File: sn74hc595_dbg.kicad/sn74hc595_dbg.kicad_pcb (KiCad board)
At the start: 2 copper layers, 27.7 x 42.8 mm, 12 parts, among them J1 Conn_01x04, J2 Conn_01x04, U2 74HC595

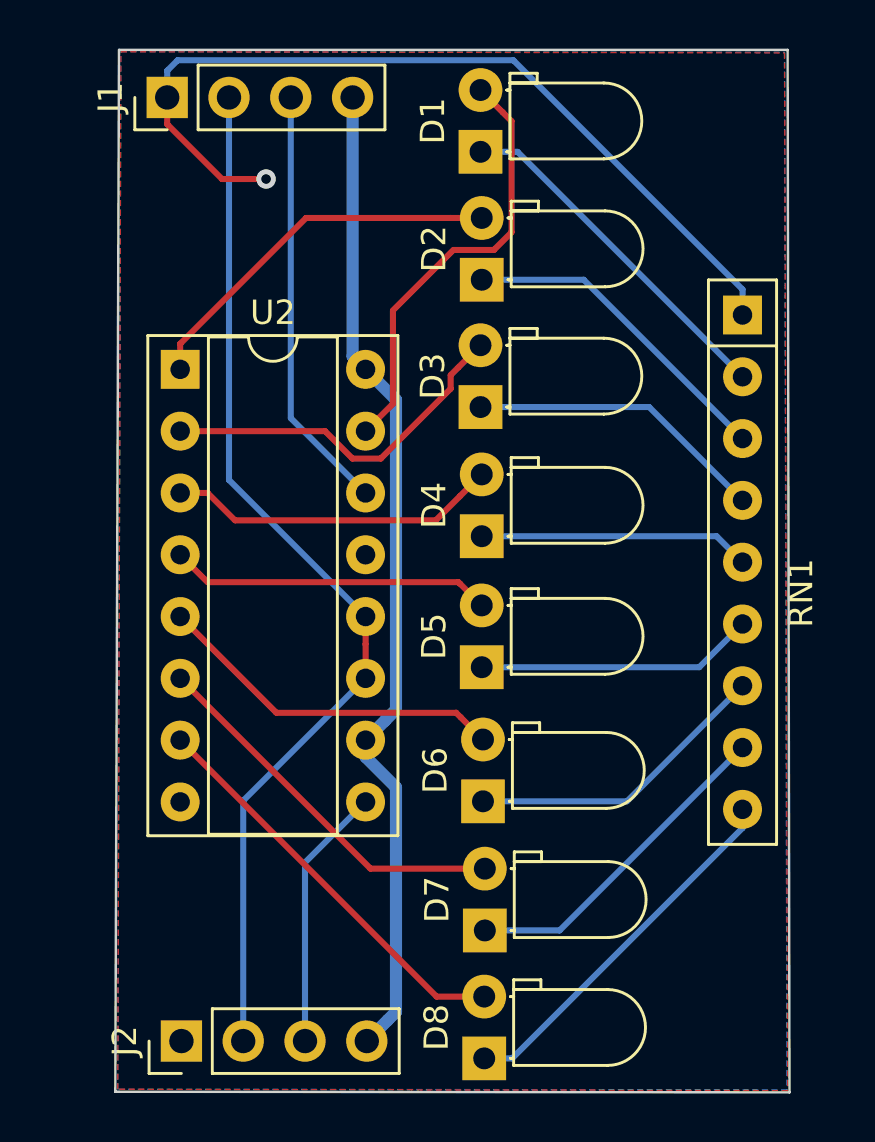
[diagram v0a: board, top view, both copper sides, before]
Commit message: swapped horizontal LEDs with vertical LEDs
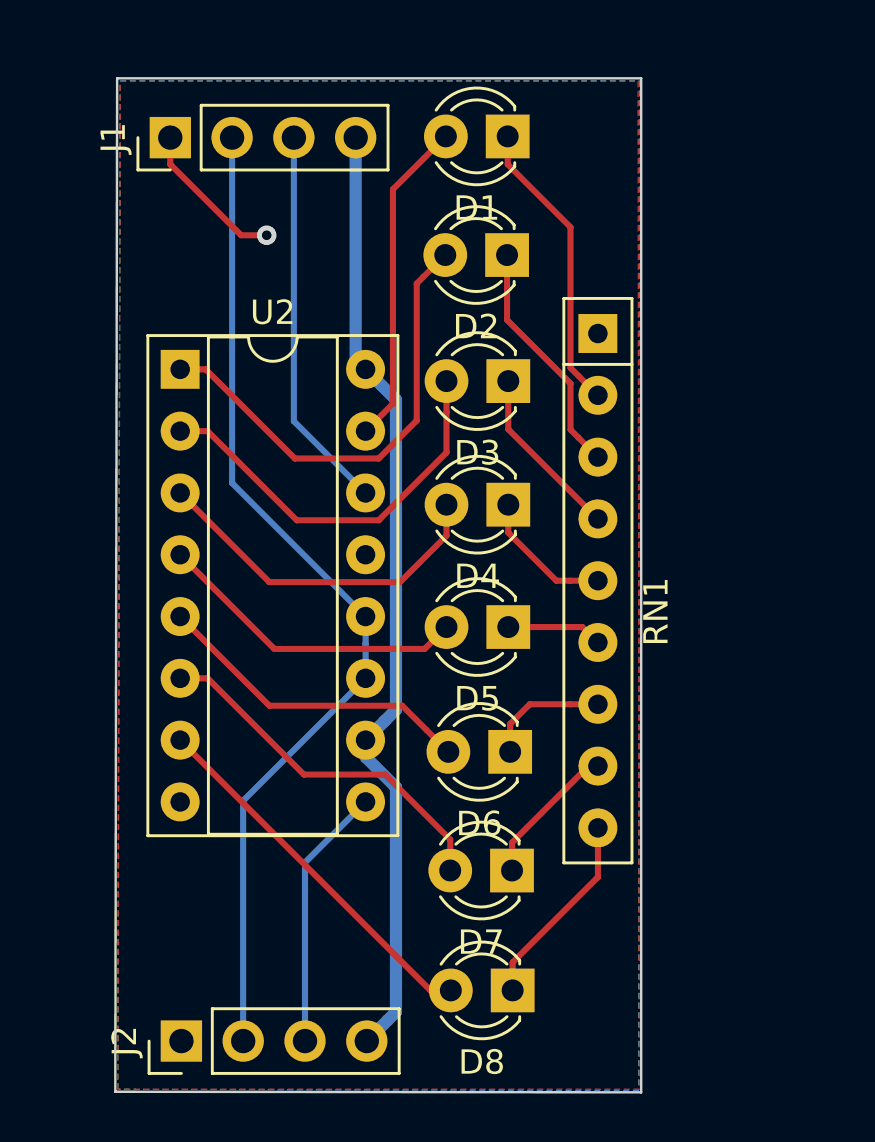
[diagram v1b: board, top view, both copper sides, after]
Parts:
- D1, D2, D3, D4, D5, D6, D7, D8: footprint LED_THT:LED_D3.0mm_Horizontal_O1.27mm_Z2.0mm_Clear -> LED_THT:LED_D3.0mm
- moved RN1 5.99 mm to (103.3, 57.9)
- moved D8 3.03 mm to (99.8, 84.9), turned to 180 degrees
- moved D7 2.71 mm to (99.7, 80.0), turned to 180 degrees
- moved D6 2.32 mm to (99.7, 75.1), turned to 180 degrees
- moved D5 1.98 mm to (99.6, 70.0), turned to 180 degrees
- moved D4 1.69 mm to (99.6, 65.0), turned to 180 degrees
- moved J1 1.66 mm to (85.7, 49.9)
- moved D3 1.56 mm to (99.6, 59.9), turned to 180 degrees
- moved D2 1.45 mm to (99.5, 54.7), turned to 180 degrees
- moved D1 1.29 mm to (99.6, 49.8), turned to 180 degrees
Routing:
- net GND: track 36.0 -> 6.27 mm
- net Net-(D7-Pad1): track 13.7 -> 5.98 mm
- net Net-(D6-Pad1): track 12.6 -> 5.09 mm
- net Net-(D5-Pad1): track 11.5 -> 3.95 mm
- net Net-(D8-Pad1): track 15.3 -> 8.13 mm
- net Net-(D4-Pad1): track 11.2 -> 5.65 mm
- net Net-(D3-Pad1): track 12.4 -> 7.19 mm
- net Net-(D1-Pad2): track 18.0 -> 13.5 mm
- net Net-(D2-Pad2): track 15.6 -> 19.2 mm
- net Net-(D2-Pad1): track 13.4 -> 9.85 mm
- net Net-(D1-Pad1): track 14.6 -> 12.2 mm
- net Net-(J1-Pad3): track 17.5 -> 15.8 mm
- net +5V: track 41.1 -> 39.4 mm
- net Net-(J1-Pad2): track 43.2 -> 41.5 mm
- net Net-(D3-Pad2): track 15.1 -> 16.6 mm
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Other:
- board size 27.7 x 42.8 mm -> 21.6 x 41.7 mm

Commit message: optimized layout, added labels
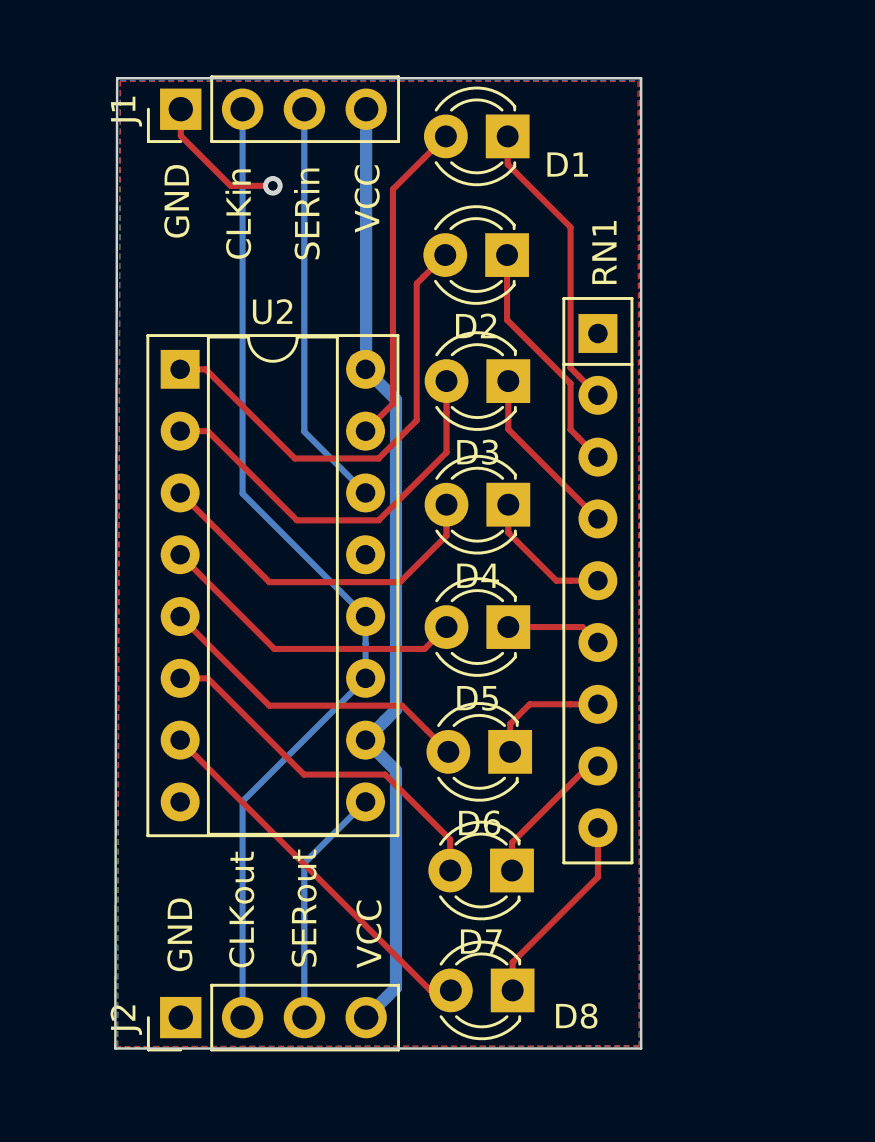
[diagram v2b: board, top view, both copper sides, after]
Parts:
- moved J1 1.25 mm to (86.1, 48.7)
- moved J2 0.97 mm to (86.1, 86.1)
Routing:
- net Net-(J1-Pad3): track 15.8 -> 16.8 mm
- net Net-(J2-Pad3): track 10.9 -> 9.91 mm
- net +5V: track 39.4 -> 40.0 mm
- net GND: track 6.27 -> 5.73 mm
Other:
- board size 21.6 x 41.7 mm -> 21.6 x 39.9 mm
- board text added: "CLKin"
- board text added: "CLKout"
- board text added: "GND"
- board text added: "Rev 1"
- board text added: "SERin"
- board text added: "SERout"
- board text added: "VCC"
- board text added: "https://github.com/ bablokb/pic-toolchain/ src/sn74hc595_dbg"

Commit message: Rev 2: connector for output-pins / jumper for SCLK/RCLK connection
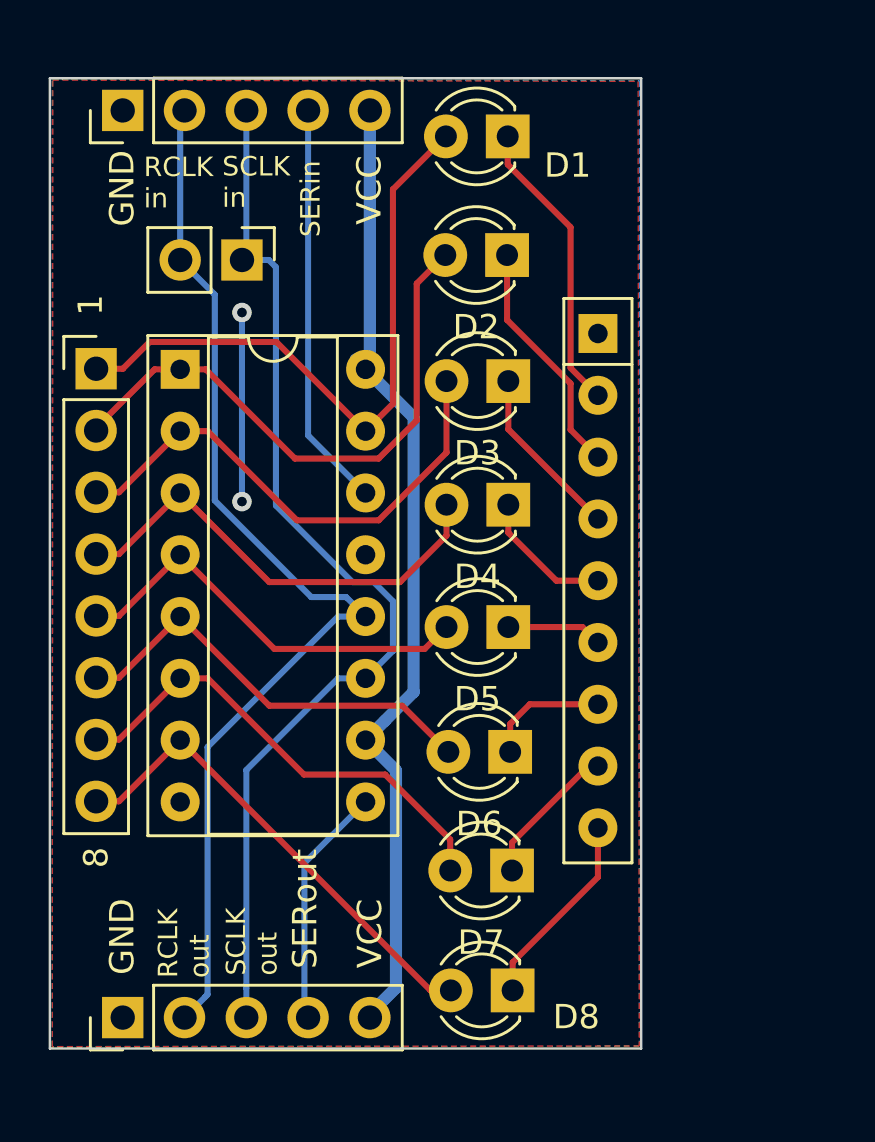
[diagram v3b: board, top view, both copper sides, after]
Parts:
- added J3: Jumper, Connector_PinHeader_2.54mm:PinHeader_1x02_P2.54mm_Vertical, F.Cu at (88.6, 54.9)
- added J4: Conn_01x08_Male, Connector_PinHeader_2.54mm:PinHeader_1x08_P2.54mm_Vertical, F.Cu at (82.7, 59.4)
- J1, J2: value Conn_01x04 -> Conn_01x05; footprint Connector_PinHeader_2.54mm:PinHeader_1x04_P2.54mm_Vertical -> Connector_PinHeader_2.54mm:PinHeader_1x05_P2.54mm_Vertical
- RN1: value R_Network08 -> 680
- moved J1 2.39 mm to (83.7, 48.8)
- moved J2 2.39 mm to (83.7, 86.1)
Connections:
- net Net-(D1-Pad2) renamed /QA
- net Net-(D2-Pad2) renamed /QB
- net Net-(D3-Pad2) renamed /QC
- net Net-(D4-Pad2) renamed /QD
- net Net-(D5-Pad2) renamed /QE
- net Net-(D6-Pad2) renamed /QF
- net Net-(D7-Pad2) renamed /QG
- net Net-(D8-Pad2) renamed /QH
- J1 pad 4: +5V -> Net-(J1-Pad4)
- J2 pad 3: Net-(J2-Pad3) -> Net-(J1-Pad3)
- J2 pad 4: +5V -> Net-(J2-Pad4)
- U2 pad 11: Net-(J1-Pad2) -> Net-(J1-Pad3)
- U2 pad 14: Net-(J1-Pad3) -> Net-(J1-Pad4)
- U2 pad 9: Net-(J2-Pad3) -> Net-(J2-Pad4)
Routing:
- net Net-(J1-Pad3): track 16.8 -> 44.2 mm
- net Net-(J1-Pad4): track 0.00 -> 16.7 mm
- net /QA: track 13.5 -> 26.5 mm
- net Net-(J2-Pad4): track 0.00 -> 9.91 mm
- net Net-(J2-Pad3): track 9.91 -> 0.00 mm
- net /QB: track 19.2 -> 23.7 mm
- net /QH: track 15.4 -> 19.9 mm
- net /QG: track 15.1 -> 19.6 mm
- net /QF: track 13.3 -> 17.8 mm
- net /QD: track 14.5 -> 19.0 mm
- net /QC: track 16.6 -> 21.1 mm
- net /QE: track 12.9 -> 17.4 mm
- net Net-(J1-Pad2): track 41.5 -> 45.2 mm
- net GND: track 5.73 -> 7.77 mm, vias 1 -> 2
- net +5V: track 40.0 -> 40.6 mm
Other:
- board size 21.6 x 39.9 mm -> 24.3 x 39.9 mm
- board text added: "1"
- board text added: "8"
- board text added: "RCLK in"
- board text added: "RCLK out"
- board text added: "Rev 2"
- board text added: "SCLK in"
- board text added: "SCLK out"
- board text added: "https://github.com/ bablokb/pic-sn74hc595"
- board text removed: "CLKin"
- board text removed: "CLKout"
- board text removed: "Rev 1"
- board text removed: "https://github.com/ bablokb/pic-toolchain/ src/sn74hc595_dbg"

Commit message: optimized labels
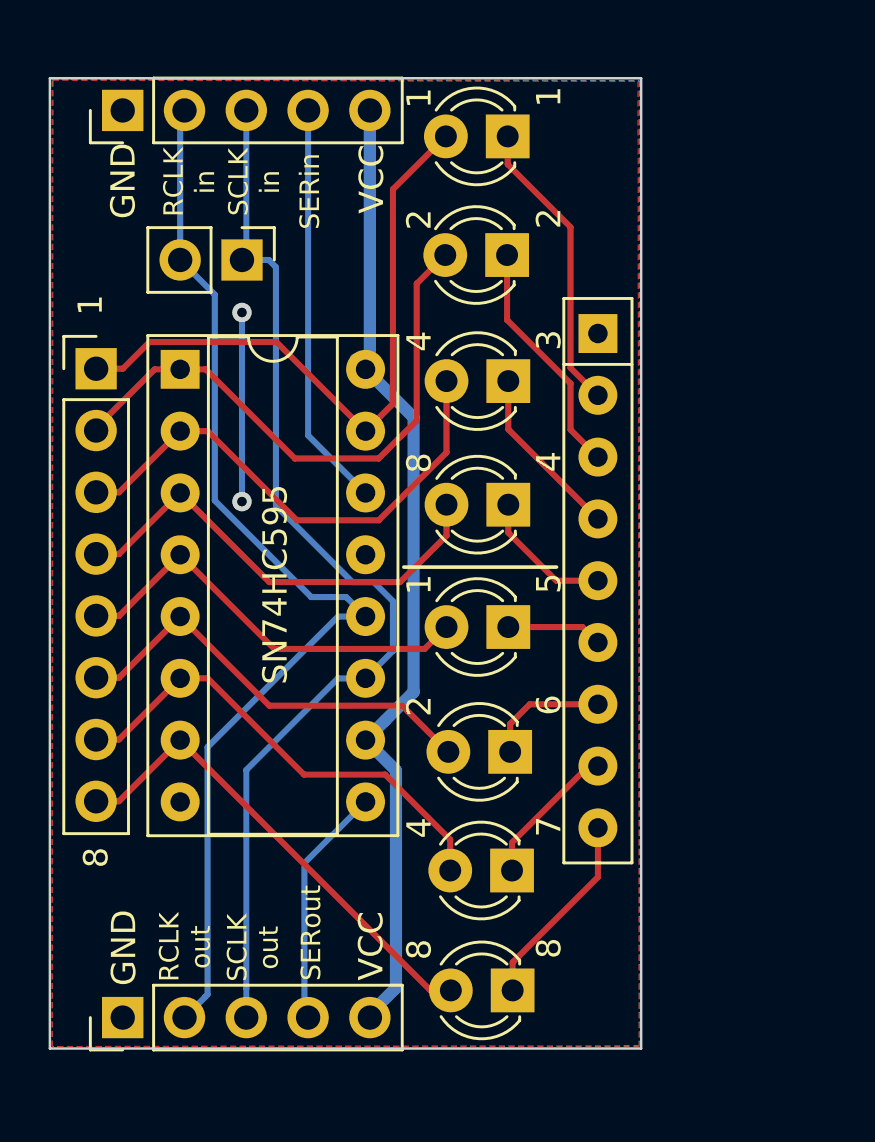
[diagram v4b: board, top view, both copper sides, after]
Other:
- board text added: "2"
- board text added: "3"
- board text added: "4"
- board text added: "5"
- board text added: "6"
- board text added: "7"
- board text added: "SN74HC595"
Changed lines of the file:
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@@
   (general
     (thickness 1.6)
-    (drawings 18)
+    (drawings 36)
     (tracks 119)
     (zones 0)
@@
   (page A4)
   (layers
-    (0 F.Cu signal)
-    (31 B.Cu signal)
+    (0 F.Cu signal hide)
+    (31 B.Cu signal hide)
     (32 B.Adhes user)
     (33 F.Adhes user)
@@
     (descr "LED, diameter 3.0mm, 2 pins")
     (tags "LED diameter 3.0mm 2 pins")
-    (fp_text reference D8 (at -2.6162 -1.0922) (layer F.SilkS)
+    (fp_text reference D8 (at -2.6162 -1.0922) (layer F.SilkS) hide
       (effects (font (size 1 1) (thickness 0.15)))
     )
@@
     (descr "LED, diameter 3.0mm, 2 pins")
     (tags "LED diameter 3.0mm 2 pins")
-    (fp_text reference D6 (at 1.27 -2.96) (layer F.SilkS)
+    (fp_text reference D6 (at 1.27 -2.96) (layer F.SilkS) hide
       (effects (font (size 1 1) (thickness 0.15)))
     )
@@
     (descr "LED, diameter 3.0mm, 2 pins")
     (tags "LED diameter 3.0mm 2 pins")
-    (fp_text reference D7 (at 1.27 -2.96) (layer F.SilkS)
+    (fp_text reference D7 (at 1.27 -2.96) (layer F.SilkS) hide
       (effects (font (size 1 1) (thickness 0.15)))
     )
@@
     (descr "LED, diameter 3.0mm, 2 pins")
     (tags "LED diameter 3.0mm 2 pins")
-    (fp_text reference D5 (at 1.27 -2.96) (layer F.SilkS)
+    (fp_text reference D5 (at 1.27 -2.96) (layer F.SilkS) hide
       (effects (font (size 1 1) (thickness 0.15)))
     )
@@
     (descr "LED, diameter 3.0mm, 2 pins")
     (tags "LED diameter 3.0mm 2 pins")
-    (fp_text reference D4 (at 1.27 -2.96) (layer F.SilkS)
+    (fp_text reference D4 (at 1.27 -2.96) (layer F.SilkS) hide
       (effects (font (size 1 1) (thickness 0.15)))
     )
@@
     (descr "LED, diameter 3.0mm, 2 pins")
     (tags "LED diameter 3.0mm 2 pins")
-    (fp_text reference D3 (at 1.27 -2.96) (layer F.SilkS)
+    (fp_text reference D3 (at 1.27 -2.96) (layer F.SilkS) hide
       (effects (font (size 1 1) (thickness 0.15)))
     )
@@
     (descr "LED, diameter 3.0mm, 2 pins")
     (tags "LED diameter 3.0mm 2 pins")
-    (fp_text reference D2 (at 1.27 -2.96) (layer F.SilkS)
+    (fp_text reference D2 (at 1.27 -2.96) (layer F.SilkS) hide
       (effects (font (size 1 1) (thickness 0.15)))
     )
@@
     (descr "LED, diameter 3.0mm, 2 pins")
     (tags "LED diameter 3.0mm 2 pins")
-    (fp_text reference D1 (at -2.4638 -1.1938) (layer F.SilkS)
+    (fp_text reference D1 (at -2.4638 -1.1938) (layer F.SilkS) hide
       (effects (font (size 1 1) (thickness 0.15)))
     )
@@
     )
   )
+  (gr_text SN74HC595 (at 90.0176 68.2498 90) (layer F.SilkS)
+    (effects (font (size 1 1) (thickness 0.15)))
+  )
+  (gr_line (start 95.3008 67.5386) (end 101.5746 67.5386) (layer F.SilkS) (width 0.15))
+  (gr_text 8 (at 95.9358 83.2578 90) (layer F.SilkS)
+    (effects (font (size 1 1) (thickness 0.15)))
+  )
+  (gr_text 4 (at 95.9358 78.2578 90) (layer F.SilkS)
+    (effects (font (size 1 1) (thickness 0.15)))
+  )
+  (gr_text 2 (at 95.9358 73.2578 90) (layer F.SilkS)
+    (effects (font (size 1 1) (thickness 0.15)))
+  )
+  (gr_text 1 (at 95.9358 68.2578 90) (layer F.SilkS)
+    (effects (font (size 1 1) (thickness 0.15)))
+  )
+  (gr_text 8 (at 95.9358 63.2578 90) (layer F.SilkS)
+    (effects (font (size 1 1) (thickness 0.15)))
+  )
+  (gr_text 4 (at 95.9358 58.2578 90) (layer F.SilkS)
+    (effects (font (size 1 1) (thickness 0.15)))
+  )
+  (gr_text 2 (at 95.9358 53.2578 90) (layer F.SilkS)
+    (effects (font (size 1 1) (thickness 0.15)))
+  )
+  (gr_text 1 (at 95.9358 48.2578 90) (layer F.SilkS)
+    (effects (font (size 1 1) (thickness 0.15)))
+  )
+  (gr_text 8 (at 101.2688 83.207 90) (layer F.SilkS)
+    (effects (font (size 1 1) (thickness 0.15)))
+  )
+  (gr_text 7 (at 101.2688 78.207 90) (layer F.SilkS)
+    (effects (font (size 1 1) (thickness 0.15)))
+  )
+  (gr_text 6 (at 101.2688 73.207 90) (layer F.SilkS)
+    (effects (font (size 1 1) (thickness 0.15)))
+  )
+  (gr_text 5 (at 101.2688 68.207 90) (layer F.SilkS)
+    (effects (font (size 1 1) (thickness 0.15)))
+  )
+  (gr_text 4 (at 101.2688 63.207 90) (layer F.SilkS)
+    (effects (font (size 1 1) (thickness 0.15)))
+  )
+  (gr_text 3 (at 101.2688 58.207 90) (layer F.SilkS)
+    (effects (font (size 1 1) (thickness 0.15)))
+  )
+  (gr_text 2 (at 101.2688 53.207 90) (layer F.SilkS)
+    (effects (font (size 1 1) (thickness 0.15)))
+  )
+  (gr_text 1 (at 101.2688 48.207 90) (layer F.SilkS)
+    (effects (font (size 1 1) (thickness 0.15)))
+  )
   (gr_text 8 (at 82.6516 79.4766 90) (layer F.SilkS)
     (effects (font (size 1 1) (thickness 0.15)))
@@
     (effects (font (size 1 1) (thickness 0.15)))
   )
-  (gr_text "RCLK\nout" (at 86.2584 84.4296 90) (layer F.SilkS)
+  (gr_text "RCLK\nout" (at 86.3092 83.1596 90) (layer F.SilkS)
+    (effects (font (size 0.8 0.8) (thickness 0.15)))
+  )
+  (gr_text SERin (at 91.44 53.6702 90) (layer F.SilkS)
     (effects (font (size 0.8 0.8) (thickness 0.15)) (justify left))
   )
-  (gr_text SERin (at 91.4654 53.975 90) (layer F.SilkS)
-    (effects (font (size 0.8 0.8) (thickness 0.15)) (justify left))
-  )
-  (gr_text "SCLK\nin" (at 87.8332 51.7144) (layer F.SilkS)
-    (effects (font (size 0.8 0.8) (thickness 0.15)) (justify left))
-  )
-  (gr_text "RCLK\nin" (at 84.6074 51.7398) (layer F.SilkS)
-    (effects (font (size 0.8 0.8) (thickness 0.15)) (justify left))
+  (gr_text "SCLK\nin" (at 89.154 51.7144 90) (layer F.SilkS)
+    (effects (font (size 0.8 0.8) (thickness 0.15)))
+  )
+  (gr_text "RCLK\nin" (at 86.487 51.7144 90) (layer F.SilkS)
+    (effects (font (size 0.8 0.8) (thickness 0.15)))
   )
   (gr_text "Rev 2" (at 102.8192 51.0286 90) (layer B.SilkS)
@@
     (effects (font (size 1 1) (thickness 0.15)) (justify left mirror))
   )
-  (gr_text GND (at 83.7184 82.7278 90) (layer F.SilkS)
-    (effects (font (size 1 1) (thickness 0.15)))
-  )
-  (gr_text "SCLK\nout" (at 89.0524 84.328 90) (layer F.SilkS)
-    (effects (font (size 0.8 0.8) (thickness 0.15)) (justify left))
-  )
-  (gr_text VCC (at 93.9038 82.6008 90) (layer F.SilkS)
-    (effects (font (size 1 1) (thickness 0.15)))
-  )
-  (gr_text SERout (at 91.2368 81.5848 90) (layer F.SilkS)
-    (effects (font (size 1 1) (thickness 0.15)))
-  )
-  (gr_text VCC (at 93.8784 52.0446 90) (layer F.SilkS)
-    (effects (font (size 1 1) (thickness 0.15)))
-  )
-  (gr_text GND (at 83.7184 51.9684 90) (layer F.SilkS)
-    (effects (font (size 1 1) (thickness 0.15)))
-  )
+  (gr_text GND (at 83.7946 83.185 90) (layer F.SilkS)
+    (effects (font (size 1 1) (thickness 0.15)))
+  )
+  (gr_text "SCLK\nout" (at 89.1032 83.185 90) (layer F.SilkS)
+    (effects (font (size 0.8 0.8) (thickness 0.15)))
+  )
+  (gr_text VCC (at 93.9546 83.1088 90) (layer F.SilkS)
+    (effects (font (size 1 1) (thickness 0.15)))
+  )
+  (gr_text SERout (at 91.4908 82.5754 90) (layer F.SilkS)
+    (effects (font (size 0.8 0.8) (thickness 0.15)))
+  )
+  (gr_text VCC (at 93.98 51.5874 90) (layer F.SilkS)
+    (effects (font (size 1 1) (thickness 0.15)))
+  )
+  (gr_text GND (at 83.7692 51.6636 90) (layer F.SilkS)
+    (effects (font (size 1 1) (thickness 0.15)))
+  )
